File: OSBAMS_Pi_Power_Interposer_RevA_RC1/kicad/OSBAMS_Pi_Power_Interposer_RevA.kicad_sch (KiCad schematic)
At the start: 2 parts, among them J1 43045-0400, J2 2x20 stacking socket

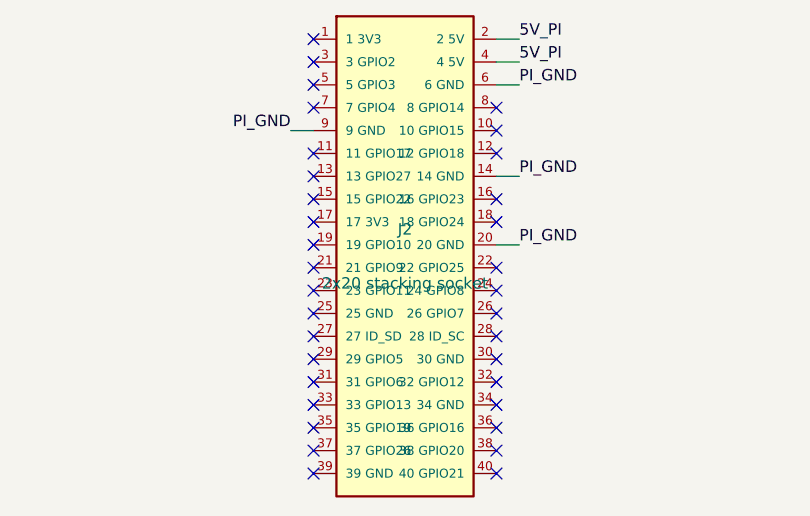
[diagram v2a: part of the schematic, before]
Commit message: Interposer around Samtec SSW-120-01-S-D; stack-height check; make_rc2 gate tool
Body 8.51 mm -> 11 mm M2.5 spacers, 20 mm key posts (+2.5 mm margin over pin tips). Socket
contact resistance stays a conservative first-article-measured placeholder. RC2 gate: only
KiCad 10 ERC remains; make_rc2.sh refuses until then.

Co-Authored-By: Claude Sonnet 5.5 <noreply@anthropic.com>
Claude-Session: https://claude.ai/code/session_01ENatZXrEDA18PaxUrZWrpi
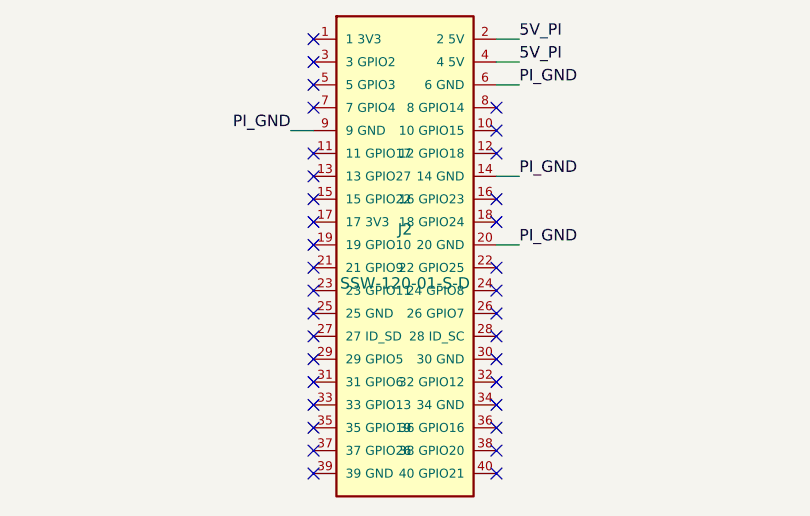
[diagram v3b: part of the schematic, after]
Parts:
- J2: value 2x20 stacking socket -> SSW-120-01-S-D; footprint OSBAMS_PiPwr:PinSocket_2x20_P2.54mm_RPi_TopView -> OSBAMS_PiPwr:SSW-120-01-S-D_RPi_TopView; MPN TBD -> SSW-120-01-S-D
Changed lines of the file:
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@@
 (symbol (lib_id "OSBAMS_PiPwr:RPi40") (at 130.00 150.00 0) (unit 1) (in_bom yes) (on_board yes) (dnp no)
   (property "Reference" "J2" (at 130.00 147.00 0) (effects (font (size 1.27 1.27))))
-  (property "Value" "2x20 stacking socket" (at 130.00 153.00 0) (effects (font (size 1.27 1.27))))
-  (property "Footprint" "OSBAMS_PiPwr:PinSocket_2x20_P2.54mm_RPi_TopView" (at 130.00 150.00 0) (effects hide))
+  (property "Value" "SSW-120-01-S-D" (at 130.00 153.00 0) (effects (font (size 1.27 1.27))))
+  (property "Footprint" "OSBAMS_PiPwr:SSW-120-01-S-D_RPi_TopView" (at 130.00 150.00 0) (effects hide))
   (property "Datasheet" "" (at 130.00 150.00 0) (effects hide))
-  (property "MPN" "TBD" (at 130.00 150.00 0) (effects hide))
+  (property "MPN" "SSW-120-01-S-D" (at 130.00 150.00 0) (effects hide))
   (pin "1")(pin "3")(pin "5")(pin "7")(pin "9")(pin "11")(pin "13")(pin "15")(pin "17")(pin "19")(pin "21")(pin "23")(pin "25")(pin "27")(pin "29")(pin "31")(pin "33")(pin "35")(pin "37")(pin "39")(pin "2")(pin "4")(pin "6")(pin "8")(pin "10")(pin "12")(pin "14")(pin "16")(pin "18")(pin "20")(pin "22")(pin "24")(pin "26")(pin "28")(pin "30")(pin "32")(pin "34")(pin "36")(pin "38")(pin "40")
   (instances (project "OSBAMS_Pi_Power_Interposer_RevA" (path "/3b1d6c7e-2a44-4f0e-8d5a-91c0a7e4b002" (reference "J2") (unit 1)))))
